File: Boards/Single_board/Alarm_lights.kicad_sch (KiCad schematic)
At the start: 46 parts, among them Q1 SI2306, Q10 SI2306, Q11 SI2306, Q12 SI2306, Q13 SI2306, Q14 SI2306, Q2 SI2306, Q3 SI2306, Q4 SI2306, Q5 SI2306, Q6 SI2306, Q7 SI2306, Q8 SI2306, Q9 SI2306, U1 PCF8575

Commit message: some progress on the arduino boilerplate
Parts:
- C2: footprint Capacitor_SMD:C_1206_3216Metric_Pad1.33x1.80mm_HandSolder -> Capacitor_SMD:C_0805_2012Metric
- D1, D10, D11, D12, D13, D14, D2, D3, D4, D5, D6, D7, D8, D9: footprint LED_SMD:LED_1206_3216Metric_Pad1.42x1.75mm_HandSolder -> LED_SMD:LED_1206_3216Metric
- Q1, Q10, Q11, Q12, Q13, Q14, Q2, Q3, Q4, Q5, Q6, Q7, Q8, Q9: footprint Package_TO_SOT_SMD:SOT-23-3 -> Package_TO_SOT_SMD:SOT-23
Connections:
- net Alt: now also U1.14 (P11); no longer U1.18 (P15)
- net Gimbal Lock: now also U1.18 (P15); no longer U1.14 (P11)
- net No Att: now also U1.6 (P2); no longer U1.10 (P6)
- net No Dap: now also U1.10 (P6); no longer U1.6 (P2)
- net Opr Err: now also U1.9 (P5); no longer U1.7 (P3)
- net Prio Disp: now also U1.11 (P7); no longer U1.5 (P1)
- net Prog: now also U1.17 (P14); no longer U1.15 (P12)
- net STBY: now also U1.7 (P3); no longer U1.9 (P5)
- net Temp: now also U1.19 (P16); no longer U1.13 (P10)
- net Tracker: now also U1.15 (P12); no longer U1.17 (P14)
- net Uplink: now also U1.5 (P1); no longer U1.11 (P7)
- net Vel: now also U1.13 (P10); no longer U1.19 (P16)

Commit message: Fixes on single board
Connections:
- net SCK renamed SCL
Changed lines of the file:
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@@
 	)
 	(junction
+		(at 60.96 220.98)
+		(diameter 0)
+		(color 0 0 0 0)
+	)
+	(junction
 		(at 33.02 171.45)
 		(diameter 0)
@@
 	(wire
 		(pts
+			(xy 60.96 220.98) (xy 60.96 222.25)
+		)
+		(stroke
+			(width 0)
+			(type default)
+		)
+	)
+	(wire
+		(pts
 			(xy 41.91 173.99) (xy 48.26 173.99)
 		)
@@
 	(wire
 		(pts
+			(xy 60.96 219.71) (xy 60.96 220.98)
+		)
+		(stroke
+			(width 0)
+			(type default)
+		)
+	)
+	(wire
+		(pts
 			(xy 203.2 58.42) (xy 209.55 58.42)
 		)
@@
 	(wire
 		(pts
+			(xy 62.23 220.98) (xy 60.96 220.98)
+		)
+		(stroke
+			(width 0)
+			(type default)
+		)
+	)
+	(wire
+		(pts
 			(xy 31.75 97.79) (xy 46.99 97.79)
 		)
@@
 		)
 	)
-	(global_label "SDA"
-		(shape input)
-		(at 29.21 173.99 180)
-		(fields_autoplaced yes)
-		(effects
-			(font
-				(size 1.27 1.27)
-			)
-			(justify right)
-		)
-		(property "Intersheetrefs" "${INTERSHEET_REFS}"
-			(at 22.6567 173.99 0)
-			(effects
-				(font
-					(size 1.27 1.27)
-				)
-				(justify right)
-				(hide yes)
-			)
-		)
-	)
 	(global_label "PWMcom"
 		(shape output)
@@
 		)
 	)
-	(global_label "SCK"
-		(shape input)
-		(at 29.21 171.45 180)
-		(fields_autoplaced yes)
-		(effects
-			(font
-				(size 1.27 1.27)
-			)
-			(justify right)
-		)
-		(property "Intersheetrefs" "${INTERSHEET_REFS}"
-			(at 22.4753 171.45 0)
-			(effects
-				(font
-					(size 1.27 1.27)
-				)
-				(justify right)
-				(hide yes)
-			)
-		)
-	)
 	(global_label "Prog"
 		(shape input)
@@
 		)
 	)
+	(hierarchical_label "GND"
+		(shape output)
+		(at 62.23 220.98 0)
+		(fields_autoplaced yes)
+		(effects
+			(font
+				(size 1.27 1.27)
+			)
+			(justify left)
+		)
+	)
+	(hierarchical_label "SCL"
+		(shape input)
+		(at 29.21 171.45 180)
+		(fields_autoplaced yes)
+		(effects
+			(font
+				(size 1.27 1.27)
+			)
+			(justify right)
+		)
+	)
+	(hierarchical_label "5V"
+		(shape input)
+		(at 30.48 157.48 90)
+		(fields_autoplaced yes)
+		(effects
+			(font
+				(size 1.27 1.27)
+			)
+			(justify left)
+		)
+	)
+	(hierarchical_label "SDA"
+		(shape bidirectional)
+		(at 29.21 173.99 180)
+		(fields_autoplaced yes)
+		(effects
+			(font
+				(size 1.27 1.27)
+			)
+			(justify right)
+		)
+	)
 	(symbol
 		(lib_id "power:+5V")
@@
 	(symbol
 		(lib_id "power:GND")
-		(at 60.96 219.71 0)
+		(at 60.96 222.25 0)
 		(unit 1)
 		(exclude_from_sim no)
@@
 		(fields_autoplaced yes)
 		(property "Reference" "#PWR08"
-			(at 60.96 226.06 0)
+			(at 60.96 228.6 0)
 			(effects
 				(font
@@
 		)
 		(property "Value" "GND"
-			(at 60.96 224.79 0)
+			(at 60.96 227.33 0)
 			(effects
 				(font
@@
 		)
 		(property "Footprint" ""
-			(at 60.96 219.71 0)
+			(at 60.96 222.25 0)
 			(effects
 				(font
@@
 		)
 		(property "Datasheet" ""
-			(at 60.96 219.71 0)
+			(at 60.96 222.25 0)
 			(effects
 				(font
@@
 		)
 		(property "Description" ""
-			(at 60.96 219.71 0)
+			(at 60.96 222.25 0)
 			(effects
 				(font

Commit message: Visual Schematic improvements
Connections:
- net PWMcom renamed PWMCom

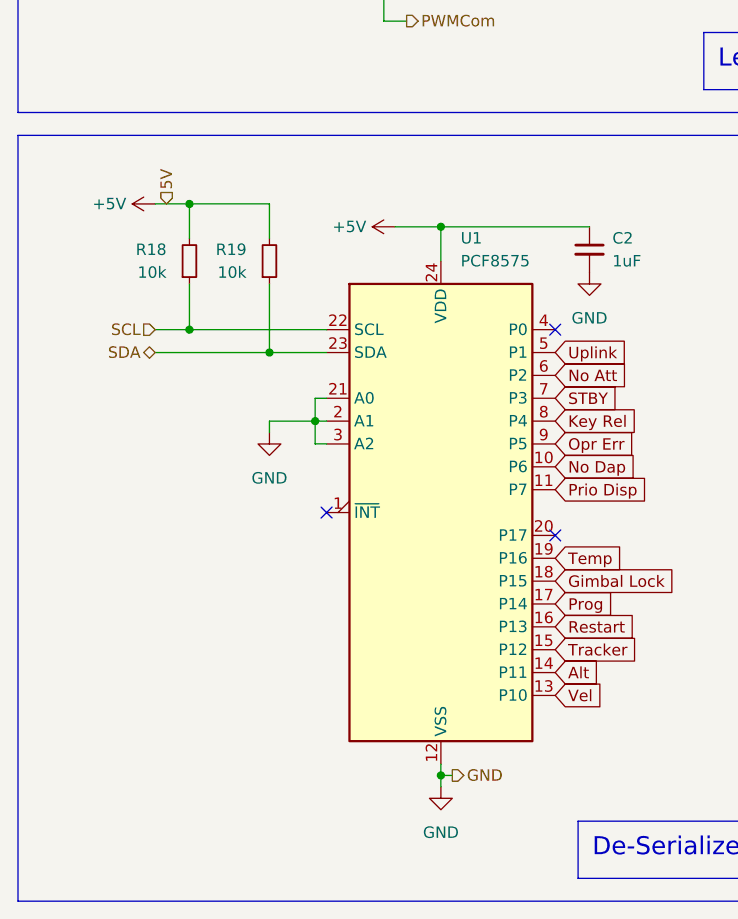
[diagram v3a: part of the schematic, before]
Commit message: Re-stitch and clean up redundant tracks.  Correct some port directions.
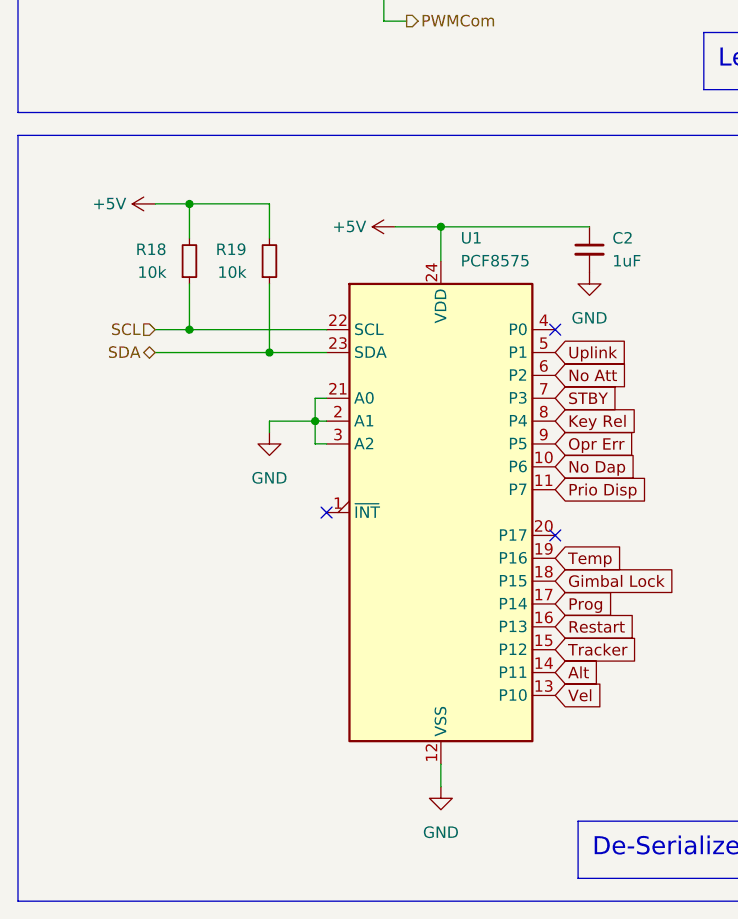
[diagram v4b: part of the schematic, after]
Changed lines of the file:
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@@
 	(generator "eeschema")
 	(generator_version "8.0")
-	(paper "A2")
+	(paper "A3")
 	(title_block
 		(title "DSKY Alarm Lights")
@@
 	)
 	(junction
-		(at 60.96 220.98)
-		(diameter 0)
-		(color 0 0 0 0)
-	)
-	(junction
 		(at 33.02 171.45)
 		(diameter 0)
@@
 	(wire
 		(pts
-			(xy 60.96 220.98) (xy 60.96 222.25)
+			(xy 60.96 219.71) (xy 60.96 222.25)
 		)
 		(stroke
@@
 	(wire
 		(pts
-			(xy 60.96 219.71) (xy 60.96 220.98)
-		)
-		(stroke
-			(width 0)
-			(type default)
-		)
-	)
-	(wire
-		(pts
 			(xy 203.2 58.42) (xy 209.55 58.42)
 		)
@@
 		(pts
 			(xy 88.9 58.42) (xy 95.25 58.42)
-		)
-		(stroke
-			(width 0)
-			(type default)
-		)
-	)
-	(wire
-		(pts
-			(xy 62.23 220.98) (xy 60.96 220.98)
 		)
 		(stroke
@@
 		)
 	)
-	(hierarchical_label "GND"
-		(shape output)
-		(at 62.23 220.98 0)
-		(fields_autoplaced yes)
-		(effects
-			(font
-				(size 1.27 1.27)
-			)
-			(justify left)
-		)
-	)
 	(hierarchical_label "PWMCom"
 		(shape output)
@@
 		)
 	)
-	(hierarchical_label "5V"
-		(shape input)
-		(at 30.48 157.48 90)
-		(fields_autoplaced yes)
-		(effects
-			(font
-				(size 1.27 1.27)
-			)
-			(justify left)
-		)
-	)

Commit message: Start RGB LED + hotswap socket redesign of single board
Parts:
- removed C2: 1uF, Capacitor_SMD:C_0805_2012Metric, symbol Device:C_Small
- removed R18, R19: 10k, Resistor_SMD:R_1206_3216Metric, symbol Device:R_Small
- removed U1: PCF8575, Package_SO:SOIC-24W_7.5x15.4mm_P1.27mm, symbol Interface_Expansion:PCF8574
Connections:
- removed net PWMCom: Q1.2 (S), Q10.2 (S), Q11.2 (S), Q12.2 (S), Q13.2 (S), Q14.2 (S), Q2.2 (S), Q3.2 (S), Q4.2 (S), Q5.2 (S), Q6.2 (S), Q7.2 (S), Q8.2 (S), Q9.2 (S)
- no-connect marks 3 -> 0
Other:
- moved on the sheet: D10, D11, D12, D13, D14, D8, D9, Q10, Q11, Q12, Q13, Q14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
